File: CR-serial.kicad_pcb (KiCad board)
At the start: 4 copper layers, 81.5 x 67.8 mm, 92 parts, among them J1 USB_B, J2 GPIO, J3 UART0, J4 UART1, J5 UART2, J6 UART3_HV, J7 RS232_0, J8 RS232_1, U1 CP2108-xxx-xM, U10 TVS4201MR6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

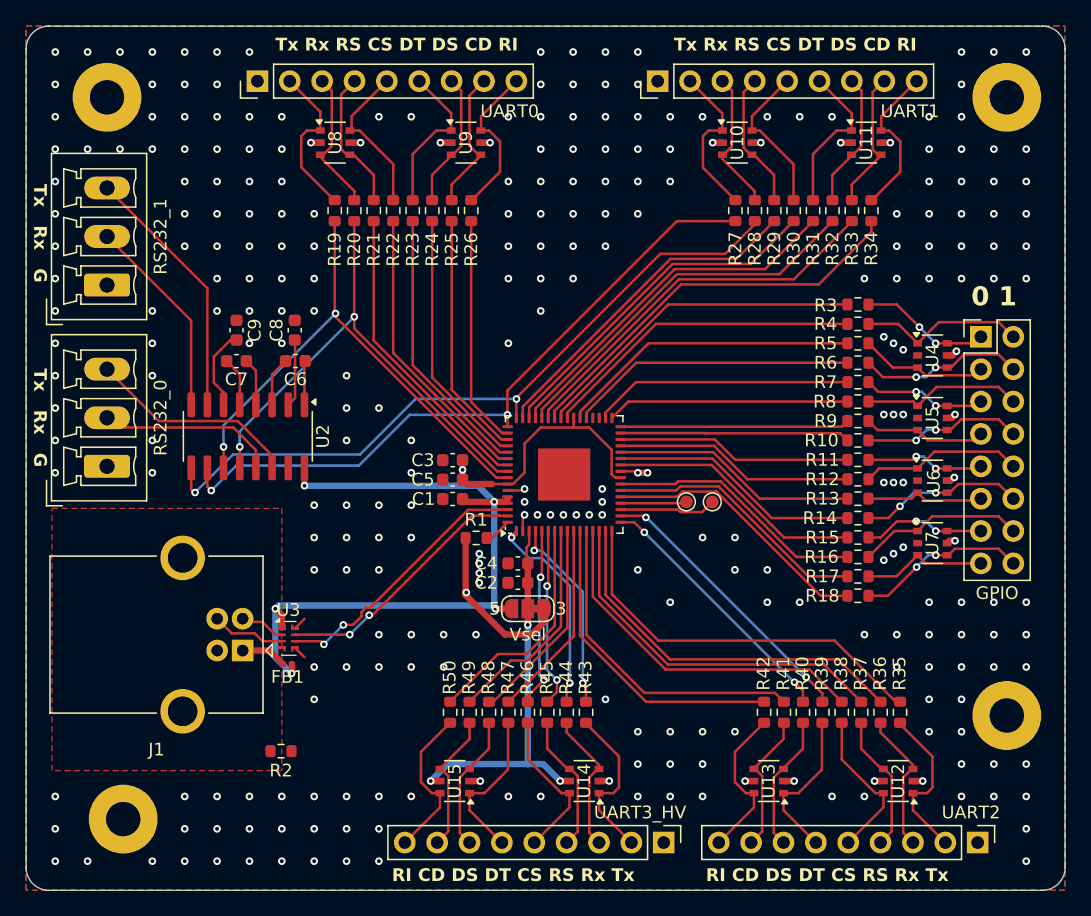
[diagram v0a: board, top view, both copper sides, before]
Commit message: More GND vias
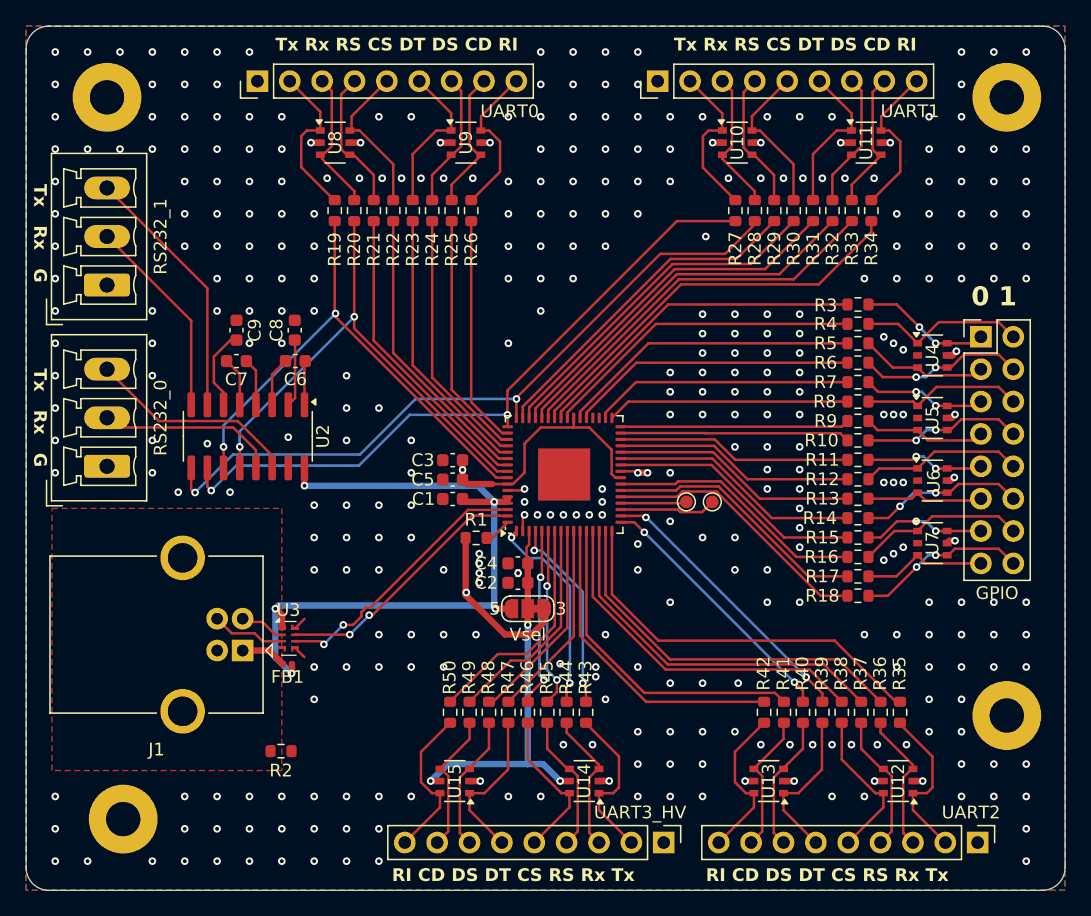
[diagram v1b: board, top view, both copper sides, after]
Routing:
- net GND: vias 280 -> 358

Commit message: PCB: Add layer indicator
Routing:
- net GND: vias 358 -> 356
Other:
- board text added: "1"
- board text added: "2"
- board text added: "3"
- board text added: "4"

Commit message: Add one more capacitor to VBUS
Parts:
- added C10: 1u, Capacitor_SMD:C_0603_1608Metric, F.Cu at (181.9, 116.3)
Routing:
- net VBUS: track 55.8 -> 57.4 mm
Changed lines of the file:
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@@
 		)
 	)
+	(footprint "Capacitor_SMD:C_0603_1608Metric"
+		(layer "F.Cu")
+		(at 181.851 116.332)
+		(descr "Capacitor SMD 0603 (1608 Metric), square (rectangular) end terminal, IPC_7351 nominal, (Body size source: IPC-SM-782 page 76, https://www.pcb-3d.com/wordpress/wp-content/uploads/ipc-sm-782a_amendment_1_and_2.pdf), generated with kicad-footprint-generator")
+		(tags "capacitor")
+		(property "Reference" "C10"
+			(at 3.061 0 0)
+			(layer "F.SilkS")
+			(effects
+				(font
+					(size 1 1)
+					(thickness 0.15)
+				)
+			)
+		)
+		(property "Value" "1u"
+			(at 0 1.43 0)
+			(layer "F.Fab")
+			(effects
+				(font
+					(size 1 1)
+					(thickness 0.15)
+				)
+			)
+		)
+		(property "Footprint" "Capacitor_SMD:C_0603_1608Metric"
+			(at 0 0 0)
+			(unlocked yes)
+			(layer "F.Fab")
+			(hide yes)
+			(effects
+				(font
+					(size 1.27 1.27)
+					(thickness 0.15)
+				)
+			)
+		)
+		(property "Datasheet" ""
+			(at 0 0 0)
+			(unlocked yes)
+			(layer "F.Fab")
+			(hide yes)
+			(effects
+				(font
+					(size 1.27 1.27)
+					(thickness 0.15)
+				)
+			)
+		)
+		(property "Description" "Polarized capacitor"
+			(at 0 0 0)
+			(unlocked yes)
+			(layer "F.Fab")
+			(hide yes)
+			(effects
+				(font
+					(size 1.27 1.27)
+					(thickness 0.15)
+				)
+			)
+		)
+		(property ki_fp_filters "CP_*")
+		(sheetname "Misc")
+		(sheetfile "misc.kicad_sch")
+		(attr smd)
+		(fp_line
+			(start -0.14058 -0.51)
+			(end 0.14058 -0.51)
+			(stroke
+				(width 0.12)
+				(type solid)
+			)
+			(layer "F.SilkS")
+		)
+		(fp_line
+			(start -0.14058 0.51)
+			(end 0.14058 0.51)
+			(stroke
+				(width 0.12)
+				(type solid)
+			)
+			(layer "F.SilkS")
+		)
+		(fp_line
+			(start -1.48 -0.73)
+			(end 1.48 -0.73)
+			(stroke
+				(width 0.05)
+				(type solid)
+			)
+			(layer "F.CrtYd")
+		)
+		(fp_line
+			(start -1.48 0.73)
+			(end -1.48 -0.73)
+			(stroke
+				(width 0.05)
+				(type solid)
+			)
+			(layer "F.CrtYd")
+		)
+		(fp_line
+			(start 1.48 -0.73)
+			(end 1.48 0.73)
+			(stroke
+				(width 0.05)
+				(type solid)
+			)
+			(layer "F.CrtYd")
+		)
+		(fp_line
+			(start 1.48 0.73)
+			(end -1.48 0.73)
+			(stroke
+				(width 0.05)
+				(type solid)
+			)
+			(layer "F.CrtYd")
+		)
+		(fp_line
+			(start -0.8 -0.4)
+			(end 0.8 -0.4)
+			(stroke
+				(width 0.1)
+				(type solid)
+			)
+			(layer "F.Fab")
+		)
+		(fp_line
+			(start -0.8 0.4)
+			(end -0.8 -0.4)
+			(stroke
+				(width 0.1)
+				(type solid)
+			)
+			(layer "F.Fab")
+		)
+		(fp_line
+			(start 0.8 -0.4)
+			(end 0.8 0.4)
+			(stroke
+				(width 0.1)
+				(type solid)
+			)
+			(layer "F.Fab")
+		)
+		(fp_line
+			(start 0.8 0.4)
+			(end -0.8 0.4)
+			(stroke
+				(width 0.1)
+				(type solid)
+			)
+			(layer "F.Fab")
+		)
+		(fp_text user "${REFERENCE}"
+			(at 0 0 0)
+			(layer "F.Fab")
+			(effects
+				(font
+					(size 0.4 0.4)
+					(thickness 0.06)
+				)
+			)
+		)
+		(pad "1" smd roundrect
+			(at -0.775 0)
+			(size 0.9 0.95)
+			(layers "F.Cu" "F.Paste" "F.Mask")
+			(roundrect_rratio 0.25)
+			(net 1 "VBUS")
+			(pintype "passive")
+		)
+		(pad "2" smd roundrect
+			(at 0.775 0)
+			(size 0.9 0.95)
+			(layers "F.Cu" "F.Paste" "F.Mask")
+			(roundrect_rratio 0.25)
+			(net 2 "GND")
+			(pintype "passive")
+		)
+		(model "${KICAD8_3DMODEL_DIR}/Capacitor_SMD.3dshapes/C_0603_1608Metric.wrl"
+			(offset
+				(xyz 0 0 0)
+			)
+			(scale
+				(xyz 1 1 1)
+			)
+			(rotate
+				(xyz 0 0 0)
+			)
+		)
+	)
 	(footprint "Resistor_SMD:R_0603_1608Metric"
 		(layer "F.Cu")
@@
 	)
 	(segment
+		(start 180.952 116.456)
+		(end 181.076 116.332)
+		(width 0.5)
+		(layer "F.Cu")
+		(net 1)
+	)
+	(segment
 		(start 178.562 132.588)
 		(end 178.6075 132.5425)
 		(width 0.5)
 		(layer "F.Cu")
+		(net 1)
+	)
+	(segment
+		(start 179.578 116.456)
+		(end 180.952 116.456)
+		(width 0.5)
+		(layer "F.Cu")

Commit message: Add option for ADM202
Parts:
- added C11: 1u, Capacitor_SMD:C_0603_1608Metric, F.Cu at (181.4, 109.7)
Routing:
- net VBUS: track 57.4 -> 63.3 mm
- net Net-(U2-VS+): track 5.31 -> 9.17 mm
- net GND: vias 356 -> 358

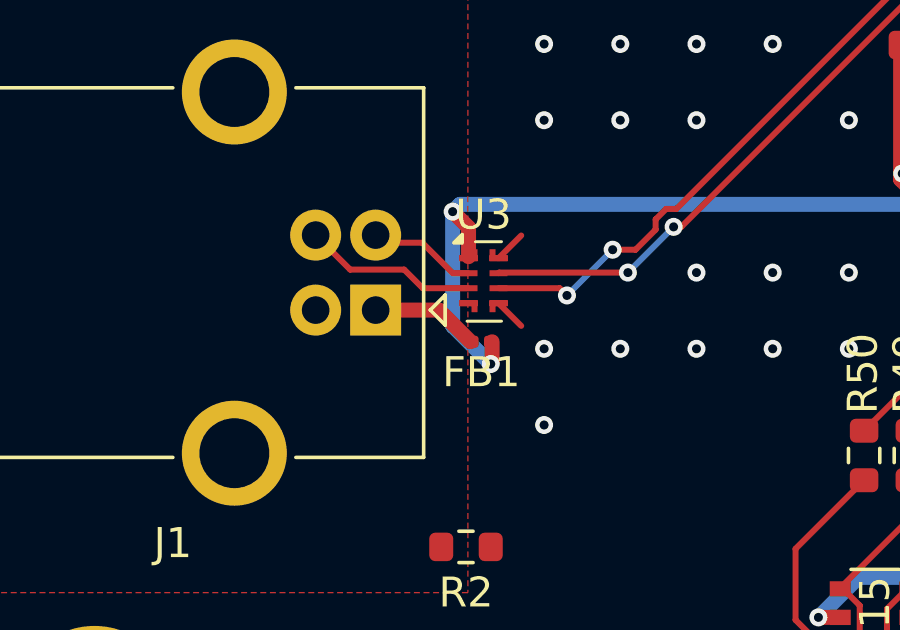
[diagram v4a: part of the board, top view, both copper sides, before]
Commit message: Update PCB: fix ferrite and 100nF capacitors
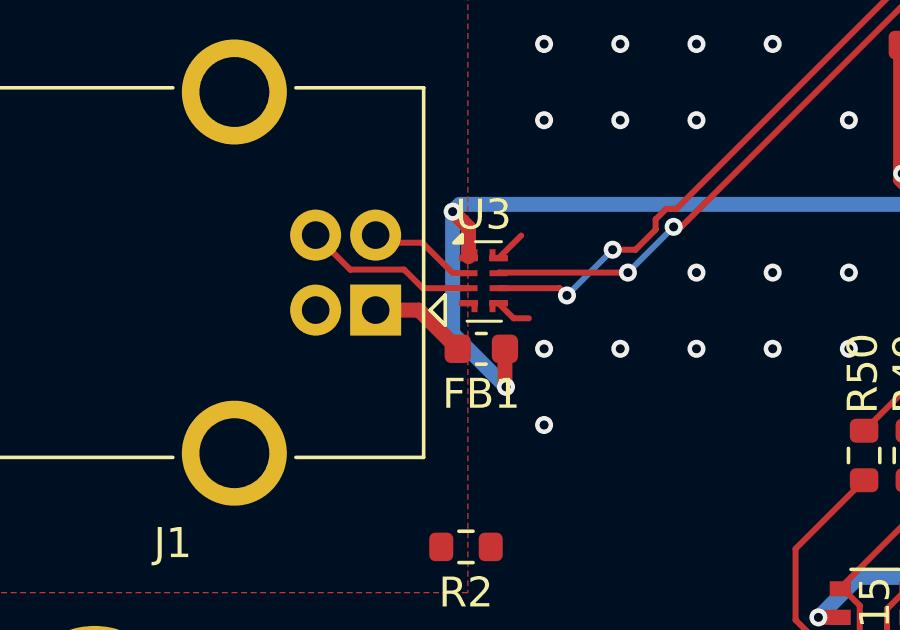
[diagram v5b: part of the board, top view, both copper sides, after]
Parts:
- C4, C5: value .1u -> 100n
- FB1: footprint Inductor_SMD:L_0201_0603Metric -> Inductor_SMD:L_0603_1608Metric
- moved FB1 0.23 mm to (178.2, 132.1)
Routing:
- net VBUS: track 63.3 -> 64.8 mm
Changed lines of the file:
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@@
 		)
 	)
-	(footprint "Inductor_SMD:L_0201_0603Metric"
+	(footprint "Inductor_SMD:L_0603_1608Metric"
 		(layer "F.Cu")
-		(at 178.2475 131.846)
-		(descr "Inductor SMD 0201 (0603 Metric), square (rectangular) end terminal, IPC_7351 nominal, (Body size source: https://www.vishay.com/docs/20052/crcw0201e3.pdf), generated with kicad-footprint-generator")
+		(at 178.2475 132.08)
+		(descr "Inductor SMD 0603 (1608 Metric), square (rectangular) end terminal, IPC_7351 nominal, (Body size source: http://www.tortai-tech.com/upload/download/2011102023233369053.pdf), generated with kicad-footprint-generator")
 		(tags "inductor")
 		(property "Reference" "FB1"
-			(at 0 1.016 0)
+			(at 0 1.504 0)
 			(layer "F.SilkS")
 			(effects
@@
 		)
 		(property "Value" "BLM18PG181SN1D"
-			(at 0 1.05 0)
+			(at 0 1.43 0)
 			(layer "F.Fab")
 			(effects
@@
 			)
 		)
-		(property "Footprint" "Inductor_SMD:L_0201_0603Metric"
+		(property "Footprint" "Inductor_SMD:L_0603_1608Metric"
 			(at 0 0 0)
 			(unlocked yes)
@@
 		(attr smd)
 		(fp_line
-			(start -0.7 -0.35)
-			(end 0.7 -0.35)
+			(start -0.162779 -0.51)
+			(end 0.162779 -0.51)
+			(stroke
+				(width 0.12)
+				(type solid)
+			)
+			(layer "F.SilkS")
+		)
+		(fp_line
+			(start -0.162779 0.51)
+			(end 0.162779 0.51)
+			(stroke
+				(width 0.12)
+				(type solid)
+			)
+			(layer "F.SilkS")
+		)
+		(fp_line
+			(start -1.48 -0.73)
+			(end 1.48 -0.73)
 			(stroke
 				(width 0.05)
@@
 		)
 		(fp_line
-			(start -0.7 0.35)
-			(end -0.7 -0.35)
+			(start -1.48 0.73)
+			(end -1.48 -0.73)
 			(stroke
 				(width 0.05)
@@
 		)
 		(fp_line
-			(start 0.7 -0.35)
-			(end 0.7 0.35)
+			(start 1.48 -0.73)
+			(end 1.48 0.73)
 			(stroke
 				(width 0.05)
@@
 		)
 		(fp_line
-			(start 0.7 0.35)
-			(end -0.7 0.35)
+			(start 1.48 0.73)
+			(end -1.48 0.73)
 			(stroke
 				(width 0.05)
@@
 		)
 		(fp_line
-			(start -0.3 -0.15)
-			(end 0.3 -0.15)
+			(start -0.8 -0.4)
+			(end 0.8 -0.4)
 			(stroke
 				(width 0.1)
@@
 		)
 		(fp_line
-			(start -0.3 0.15)
-			(end -0.3 -0.15)
+			(start -0.8 0.4)
+			(end -0.8 -0.4)
 			(stroke
 				(width 0.1)
@@
 		)
 		(fp_line
-			(start 0.3 -0.15)
-			(end 0.3 0.15)
+			(start 0.8 -0.4)
+			(end 0.8 0.4)
 			(stroke
 				(width 0.1)
@@
 		)
 		(fp_line
-			(start 0.3 0.15)
-			(end -0.3 0.15)
+			(start 0.8 0.4)
+			(end -0.8 0.4)
 			(stroke
 				(width 0.1)
@@
 		)
 		(fp_text user "${REFERENCE}"
-			(at 0 -0.68 0)
+			(at 0 0 0)
 			(layer "F.Fab")
 			(effects
 				(font
-					(size 0.25 0.25)
-					(thickness 0.04)
+					(size 0.4 0.4)
+					(thickness 0.06)
 				)
 			)
 		)
-		(pad "" smd roundrect
-			(at -0.345 0)
-			(size 0.318 0.36)
-			(layers "F.Paste")
-			(roundrect_rratio 0.25)
-		)
-		(pad "" smd roundrect
-			(at 0.345 0)
-			(size 0.318 0.36)
-			(layers "F.Paste")
-			(roundrect_rratio 0.25)
-		)
 		(pad "1" smd roundrect
-			(at -0.32 0)
-			(size 0.46 0.4)
-			(layers "F.Cu" "F.Mask")
+			(at -0.7875 0)
+			(size 0.875 0.95)
+			(layers "F.Cu" "F.Paste" "F.Mask")
 			(roundrect_rratio 0.25)
 			(net 11 "Net-(J1-VBUS)")
@@
 		)
 		(pad "2" smd roundrect
-			(at 0.32 0)
-			(size 0.46 0.4)
-			(layers "F.Cu" "F.Mask")
+			(at 0.7875 0)
+			(size 0.875 0.95)
+			(layers "F.Cu" "F.Paste" "F.Mask")
 			(roundrect_rratio 0.25)
 			(net 1 "VBUS")
 			(pintype "passive")
 		)
-		(model "${KICAD8_3DMODEL_DIR}/Inductor_SMD.3dshapes/L_0201_0603Metric.wrl"
+		(model "${KICAD8_3DMODEL_DIR}/Inductor_SMD.3dshapes/L_0603_1608Metric.wrl"
 			(offset
 				(xyz 0 0 0)
@@
 			)
 		)
+		(property ki_fp_filters "CP_*")
+		(sheetname "Misc")
+		(sheetfile "misc.kicad_sch")
 		(attr smd)
 		(fp_line
@@
 			)
 		)
-		(property "Value" ".1u"
+		(property "Value" "100n"
 			(at 0 1.43 180)
 			(layer "F.Fab")
@@
 			)
 		)
-		(property "Value" ".1u"
+		(property "Value" "100n"
 			(at 0 1.43 180)
 			(layer "F.Fab")
@@
 	)
 	(segment
-		(start 178.562 132.588)
-		(end 178.6075 132.5425)
+		(start 179.07 133.35)
+		(end 179.035 133.315)
+		(width 0.5)
+		(layer "F.Cu")
+		(net 1)
+	)
+	(segment
+		(start 179.035 133.315)
+		(end 179.035 132.08)
 		(width 0.5)
 		(layer "F.Cu")
@@
 	)
 	(segment
-		(start 178.6075 132.5425)
-		(end 178.6075 131.846)
-		(width 0.5)
-		(layer "F.Cu")
-		(net 1)
-	)
-	(segment
 		(start 181.356 116.052)
 		(end 181.076 116.332)
@@
 	)
 	(via
-		(at 178.562 132.588)
+		(at 179.07 133.35)
 		(size 0.6)
 		(drill 0.3)
@@
 	)
 	(segment
+		(start 177.292 131.572)
+		(end 177.292 127.508)
+		(width 0.5)
+		(layer "B.Cu")
+		(net 1)
+	)
+	(segment
 		(start 177.292 127.508)
 		(end 177.534 127.266)
@@
 	)
 	(segment
-		(start 177.292 131.318)
-		(end 177.292 127.508)
-		(width 0.5)
-		(layer "B.Cu")
-		(net 1)
-	)
-	(segment
-		(start 178.562 132.588)
-		(end 177.292 131.318)
+		(start 179.07 133.35)
+		(end 177.292 131.572)
 		(width 0.5)
 		(layer "B.Cu")
@@
 	)
 	(segment
+		(start 178.8215 130.56)
+		(end 179.3255 131.064)
+		(width 0.2)
+		(layer "F.Cu")
+		(net 2)
+	)
+	(segment
 		(start 202.692 141.033)
 		(end 202.700278 141.024722)
@@
 	)
 	(segment
-		(start 178.8215 130.56)
-		(end 179.578 131.3165)
-		(width 0.2)
-		(layer "F.Cu")
-		(net 2)
-	)
-	(segment
 		(start 191.092 90.932)
 		(end 190.246 90.932)
@@
 	)
 	(segment
+		(start 179.3255 131.064)
+		(end 179.832 131.064)
+		(width 0.2)
+		(layer "F.Cu")
+		(net 2)
+	)
+	(segment
 		(start 204.3955 116.7245)
 		(end 205.6245 116.7245)
@@
 	)
 	(segment
-		(start 176.8315 130.79)
-		(end 177.8875 131.846)
+		(start 174.7255 130.79)
+		(end 176.17 130.79)
 		(width 0.5)
 		(layer "F.Cu")
@@
 	)
 	(segment
-		(start 174.7255 130.79)
-		(end 176.8315 130.79)
+		(start 176.17 130.79)
+		(end 177.46 132.08)
 		(width 0.5)
 		(layer "F.Cu")
@@
 	)
 	(group "USB"
-		(members "01542230-4642-4e35-8641-5ad2ec4f1534" "08bb78cd-7e2a-4ed7-a080-23f309ad57b1"
-			"0b46d1c1-3729-473f-bf61-3c08b2f03281" "1915d716-5183-4dc2-91a2-45906e2ade72"
-			"27e2bf80-b2a4-452c-a6fa-5b1b400e7310" "3b11e6fd-63bd-418f-8e75-0a910909d3bc"
-			"40d03163-49ca-43b8-985a-5fac2d42ba17" "44a6e3dc-e2cc-4732-acd7-4fa592b4a26b"
-			"57f9e713-ea3e-41fd-baee-288523ae2f95" "65959d0b-70b9-43ce-89f9-b37b4ce1c2a2"
-			"67156972-5b0c-48d1-bcb8-71cd4bd8895c" "675eef17-7292-4d75-b4a6-43abae126ba0"
-			"6ddfa344-ae19-4dd2-9a67-80f9a6ae41f0" "75802594-2909-4277-aea0-6fcefd25bbd0"
-			"82a6a782-a1a5-4304-91ed-ccabdd701983" "8b258deb-481a-40f4-acc7-ca70d62d537f"
+		(members "01542230-4642-4e35-8641-5ad2ec4f1534" "04082dff-dfbe-4ab3-bd01-5ddc0b00798f"
+			"08bb78cd-7e2a-4ed7-a080-23f309ad57b1" "0b46d1c1-3729-473f-bf61-3c08b2f03281"
+			"0dcaf2fc-704e-4826-979e-a2bcb60a2e10" "1915d716-5183-4dc2-91a2-45906e2ade72"
+			"2124be21-ad99-4de7-8363-88282e432ea1" "27e2bf80-b2a4-452c-a6fa-5b1b400e7310"
+			"3b11e6fd-63bd-418f-8e75-0a910909d3bc" "40d03163-49ca-43b8-985a-5fac2d42ba17"
+			"57f9e713-ea3e-41fd-baee-288523ae2f95" "58006b14-169a-431c-b05a-9ce565e7298d"
+			"65b65f5f-2a30-4f6e-b267-c19b80db8862" "67156972-5b0c-48d1-bcb8-71cd4bd8895c"
+			"6ddfa344-ae19-4dd2-9a67-80f9a6ae41f0" "730d9225-e128-4145-bb87-91cc94fe0389"
+			"75802594-2909-4277-aea0-6fcefd25bbd0" "8b258deb-481a-40f4-acc7-ca70d62d537f"
 			"918e6fd3-e36e-4bc8-b30d-e77208c22c4e" "a843515d-2682-420f-9f08-b21154c02fc4"
 			"aae74839-b23f-455c-8907-930a08fdc0ee" "ce2bb41b-72f8-416a-b2ce-1d2c77fde7c5"
-			"cebd5642-3436-4565-b3fa-83255bd04a78" "dc66fd02-63de-43ba-9fb9-99d5202b7d29"
-			"eae67164-d7aa-47f3-a7c6-41774ffd4c6b" "ee4e85bf-9971-41a1-8dc8-66235324eda0"
+			"dc66fd02-63de-43ba-9fb9-99d5202b7d29" "eae67164-d7aa-47f3-a7c6-41774ffd4c6b"
 			"fd51f5c5-6303-4c26-9eb0-dd011047688e"
 		)
